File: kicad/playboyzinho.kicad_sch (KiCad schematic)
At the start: 3 parts, among them U1 esp32-s3-pl, U2 CR2013-MI2120, U3 MT3608

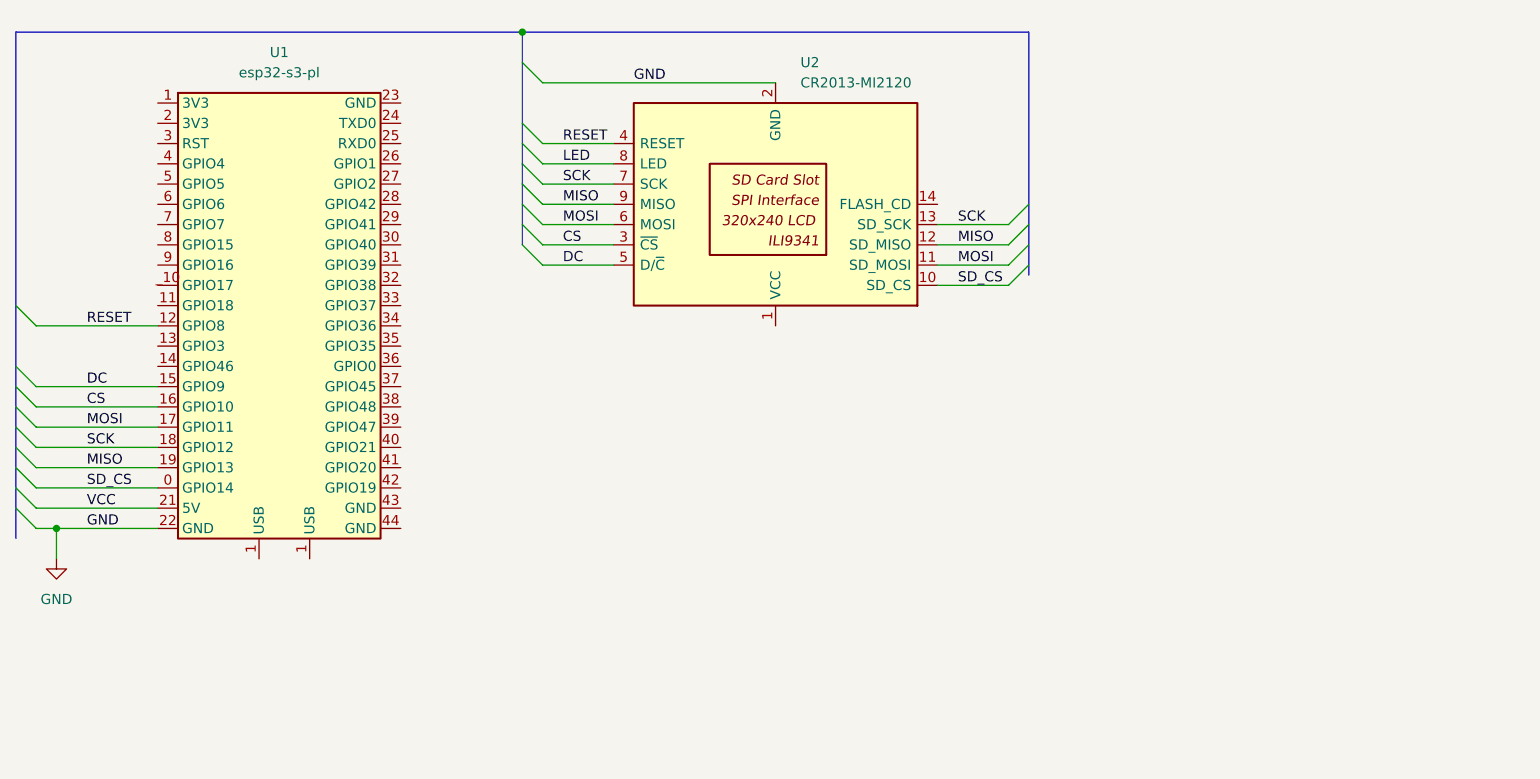
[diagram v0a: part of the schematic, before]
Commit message: feat: adicionando modulo de som no kicad
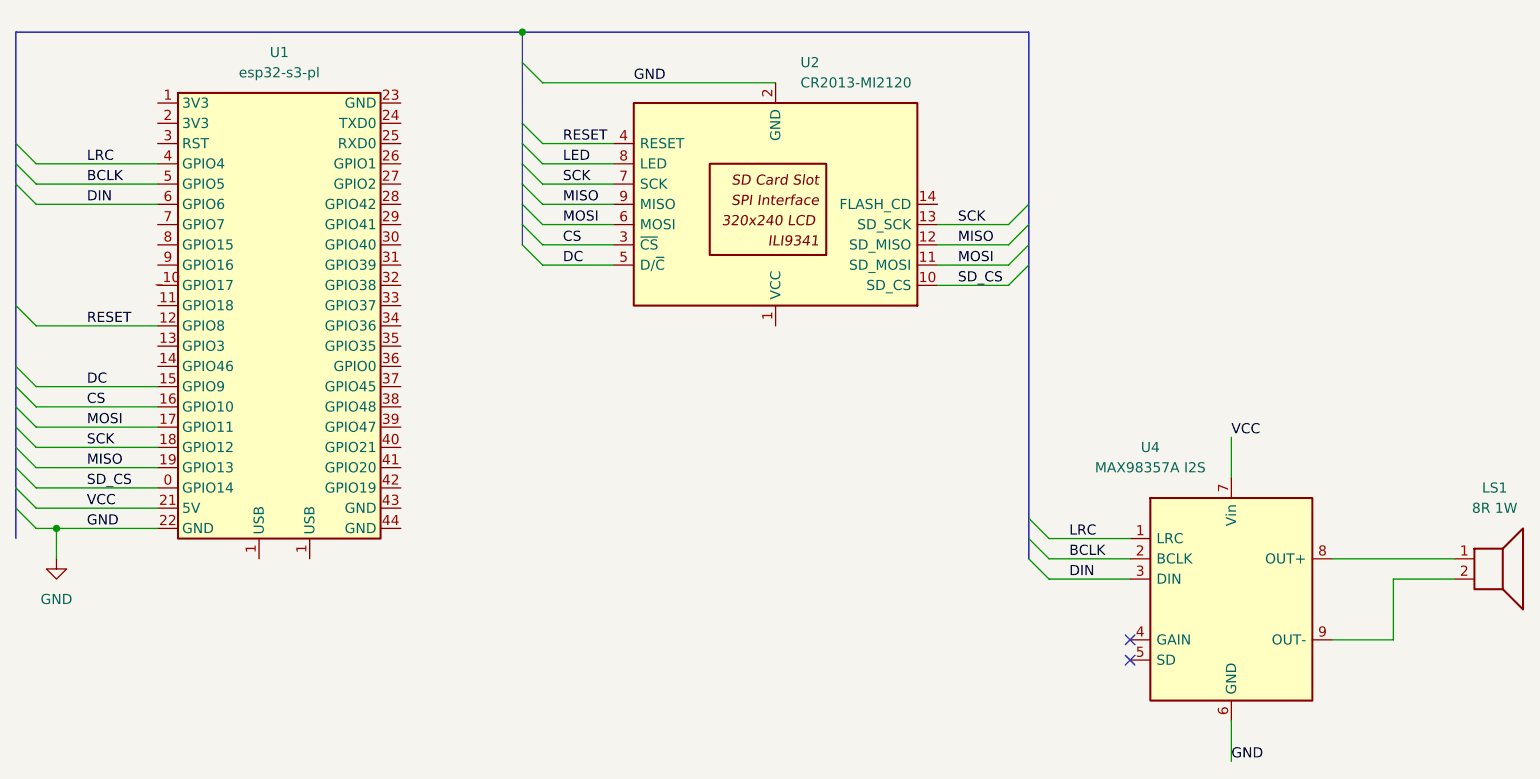
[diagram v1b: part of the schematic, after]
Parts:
- added LS1: 8R 1W, symbol Device:Speaker
- added U4: MAX98357A I2S, symbol lib-do-playboy:max98357-mod
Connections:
- net GND: now also U4.6 (GND)
- net VCC: now also U4.7 (Vin)
- net LRC: now reaches U1.4 (GPIO4)
- net LRC: now also U4.1 (LRC)
- net BCLK: now reaches U1.5 (GPIO5)
- net BCLK: now also U4.2 (BCLK)
- net DIN: now reaches U1.6 (GPIO6)
- net DIN: now also U4.3 (DIN)
- new net: LS1.1, U4.8 (OUT+)
- new net: LS1.2, U4.9 (OUT-)
- no-connect marks 0 -> 2

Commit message: feat: atualiza esquemático de acordo com circuito atualmente (28/09/2026, 6:00)
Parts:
- removed U3: MT3608, Package_TO_SOT_SMD:SOT-23-6, symbol Regulator_Switching:MT3608
- added BT1: Battery_Cell, Package_SON:Texas_DRC0010J_ThermalVias, symbol Device:Battery_Cell
- added SW1: SW_SPDT, Package_SON:WSON-8-1EP_6x5mm_P1.27mm_EP3.4x4mm, symbol Switch:SW_SPDT
- added U3: (no value), Converter_DCDC:Converter_DCDC_TRACO_TSR0.5-24xx_TSR0.5-24xxx_THT, symbol lib-do-playboy:(DC_DC)_MT3608
- added U5: (no value), Package_SO:SOIC-8-1EP_3.9x4.9mm_P1.27mm_EP2.41x3.3mm_ThermalVias, symbol lib-do-playboy:(Carregador)_TP4056
- added U6: (no value), symbol lib-do-playboy:Indicador-Bateria
- LS1: value 8R 1W -> (Speaker) 8R 1W
- U2: value CR2013-MI2120 -> (Tela 2.8) CR2013-MI2120
- U4: value MAX98357A I2S -> (Amplificador) MAX98357A I2S
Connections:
- net VCC is gone; now on net +5V: U1.21 (5V), U4.7 (Vin)
- net GND: now also U3.2 (VIN-), U3.3 (VOUT-), U5.5 (OUT-)
- net +5V: now reaches U2.1 (VCC)
- net +5V: now also U3.4 (VOUT+)
- new net: U3.1 (VIN+), U5.6 (OUT+)
- new net +BATT: BT1.1 (+), SW1.1 (A), U5.4 (B+), U6.1 (+)
- new net -BATT: BT1.2 (-), SW1.2 (B), U5.3 (B-), U6.2 (-)
- no-connect marks 2 -> 4
